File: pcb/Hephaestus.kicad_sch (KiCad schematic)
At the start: 40 parts

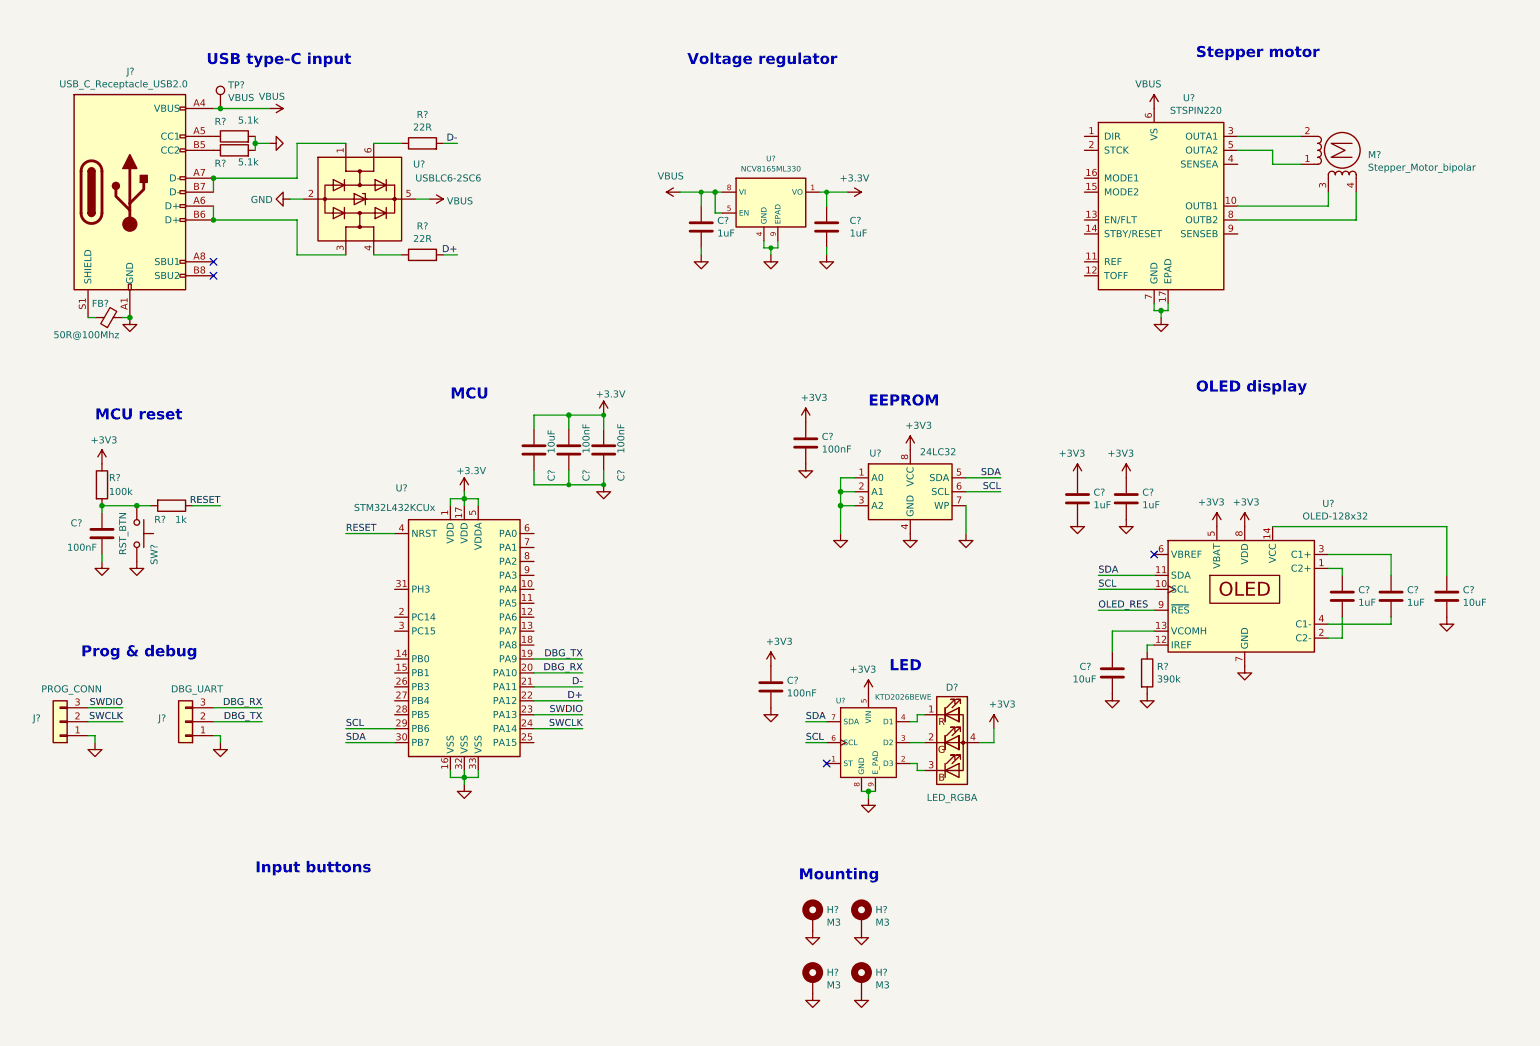
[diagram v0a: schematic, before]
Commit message: Schema: add in put buttons and denoising
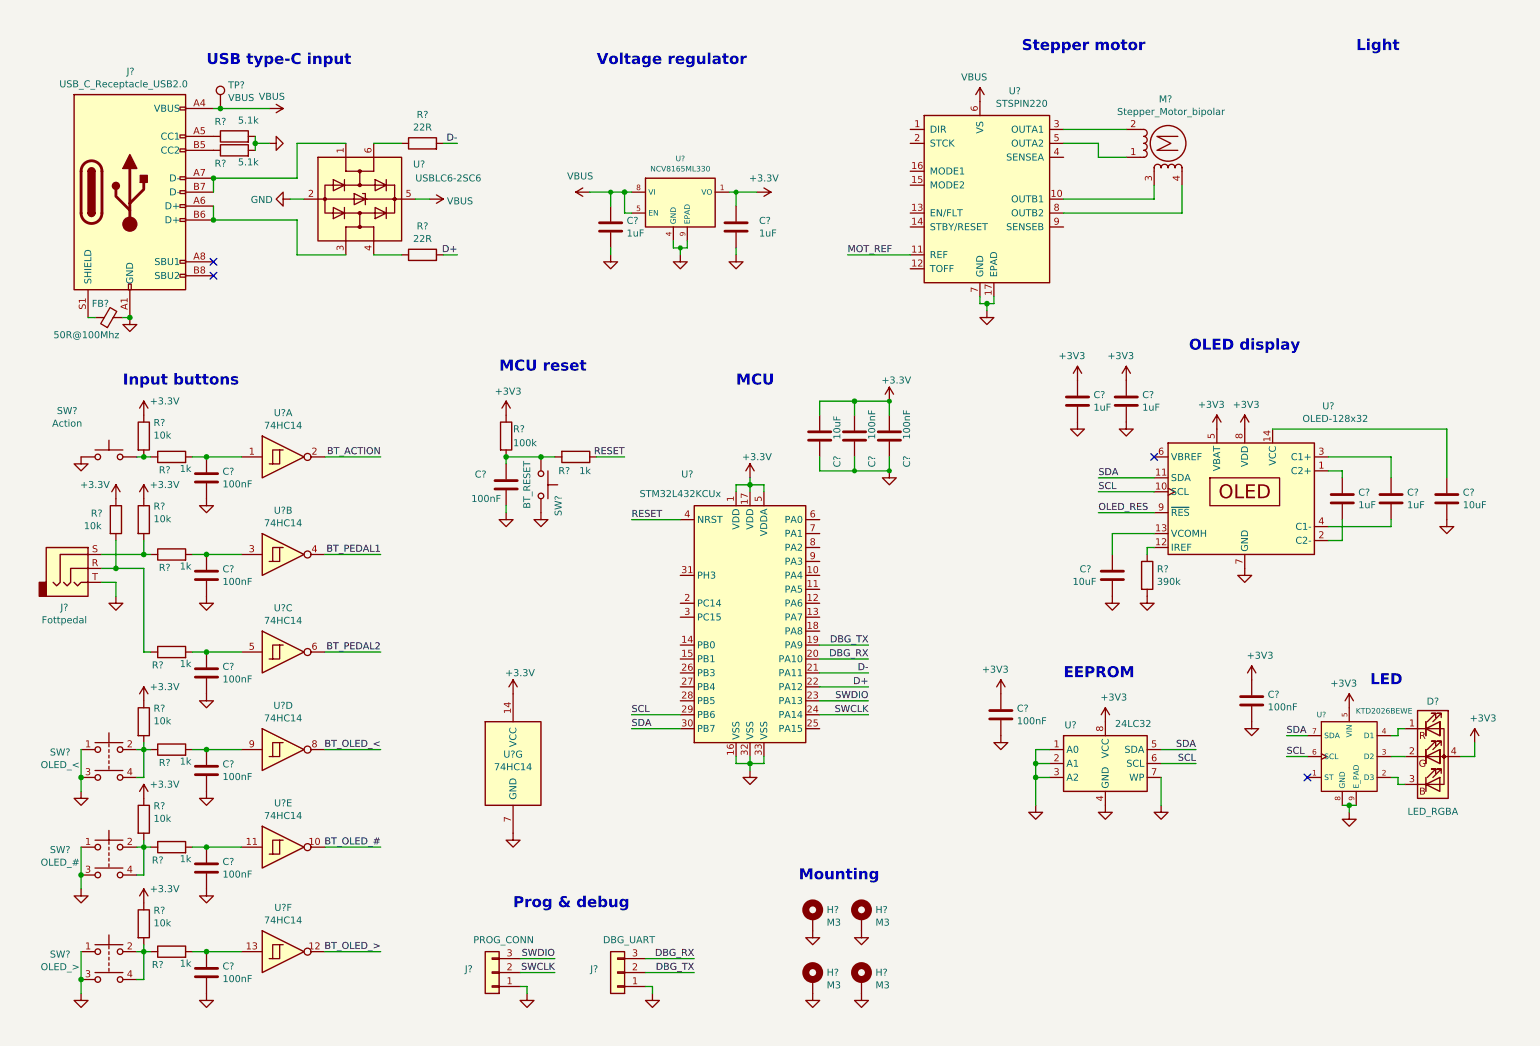
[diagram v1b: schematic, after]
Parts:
- added C? (x6): 100nF, TCY_passives:C_0603_1608Metric, symbol Device:C
- added J?: Fottpedal, Connector_Audio:Jack_3.5mm_CUI_SJ-3523-SMT_Horizontal, symbol Connector:AudioJack3
- added R? (x6): 10k, symbol Device:R
- added R? (x6): 1k, TCY_passives:R_0603_1608Metric, symbol Device:R
- added SW?: OLED_>, symbol Switch:SW_Push_Dual
- added SW?: OLED_<, symbol Switch:SW_Push_Dual
- added SW?: OLED_#, symbol Switch:SW_Push_Dual
- added SW?: Action, symbol Switch:SW_Push
- added U? (x6): 74HC14, symbol 74xx:74HC14
- added U?: 74HC14, Package_DFN_QFN:Texas_S-PVQFN-N14, symbol 74xx:74HC14
- SW?: value RST_BTN -> BT_RESET
- U?: footprint (none) -> TCY_display:OLED_128x32
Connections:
- net +3V3: now also R?.1, R?.1, R?.1, R?.1, R?.1, R?.1, U?.14 (VCC)
- net GND: now also C?.2, C?.2, C?.2, C?.2, C?.2, C?.2, J?.T, SW?.1, SW?.1, SW?.1, SW?.1, SW?.3, SW?.3, SW?.3, U?.7 (GND)
- net MOT_REF: now reaches U?.11 (REF)
- new net: R?.1, R?.2, SW?.2, SW?.4 (x3)
- new net: C?.1, R?.2, U?.9
- new net: C?.1, R?.2, U?.11
- new net: J?.S, R?.1, R?.2
- new net: J?.R, R?.1, R?.2
- new net: C?.1, R?.2, U?.5
- new net: R?.1, R?.2, SW?.2
- new net: C?.1, R?.2, U?.1
- new net: C?.1, R?.2, U?.13
- new net: C?.1, R?.2, U?.3
- new net BT_ACTION: U?.2
- new net BT_OLED_#: U?.10
- new net BT_OLED_<: U?.8
- new net BT_OLED_>: U?.12
- new net BT_PEDAL1: U?.4
- new net BT_PEDAL2: U?.6
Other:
- note added: "Light"
- moved on the sheet: C?, D?, J?, M?, R?, SW?, U?

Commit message: Schema: add light connector
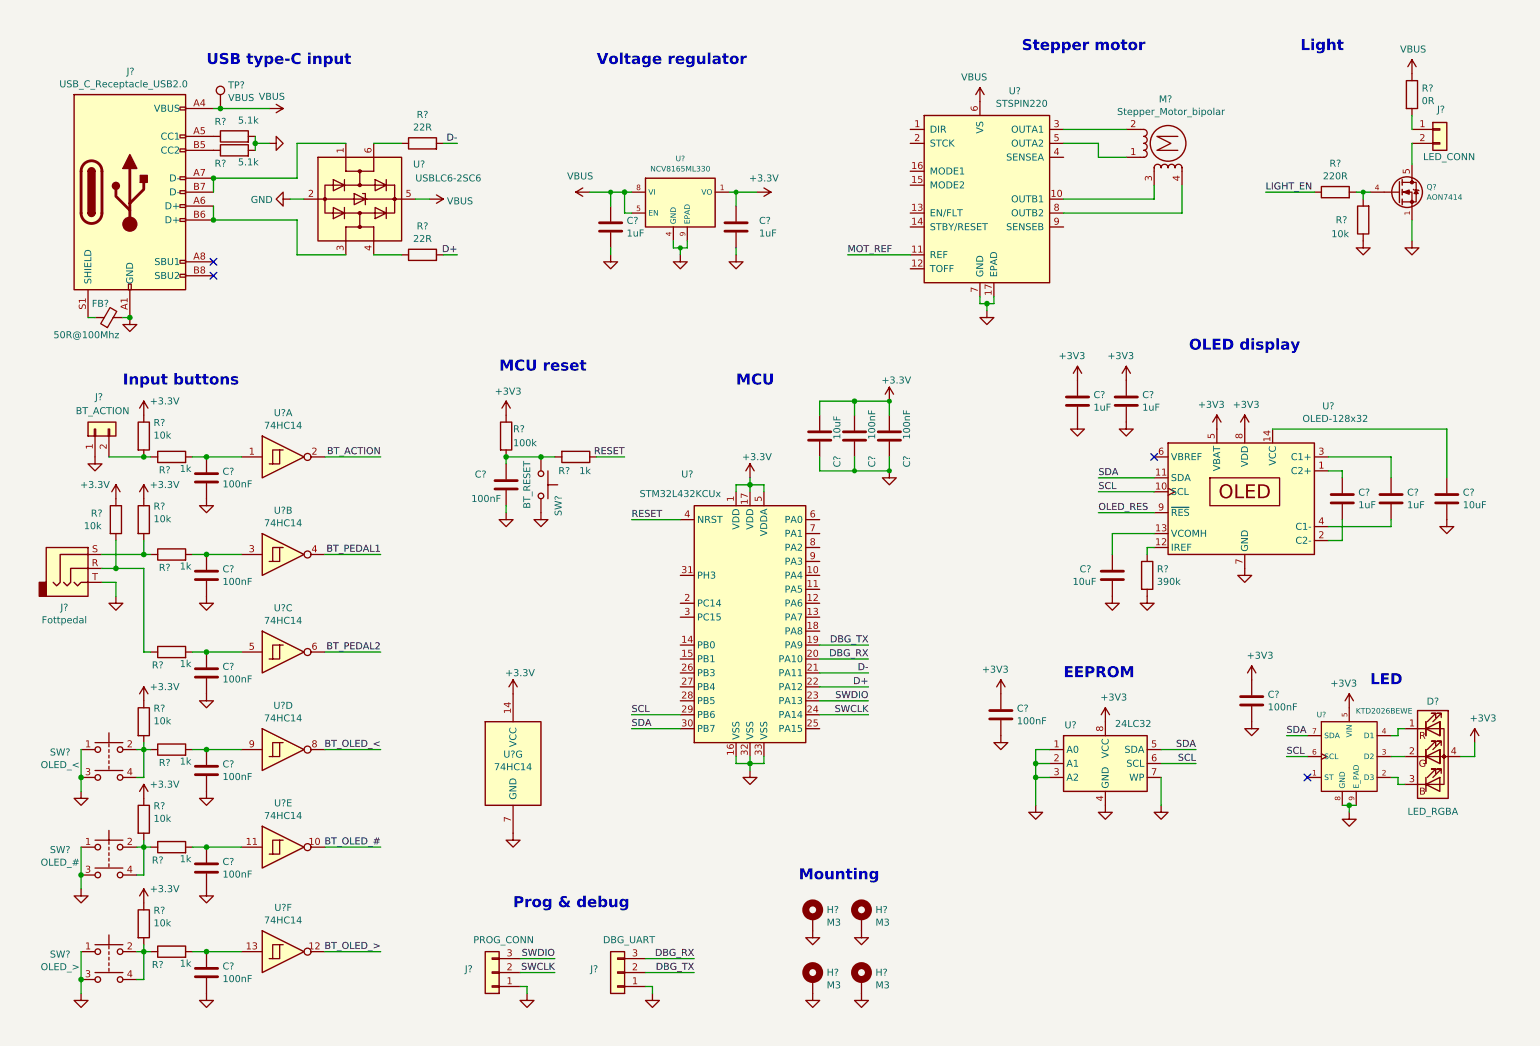
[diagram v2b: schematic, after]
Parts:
- removed SW?: Action, symbol Switch:SW_Push
- added J?: BT_ACTION, symbol Connector_Generic:Conn_01x02
- added J?: LED_CONN, symbol Connector_Generic:Conn_01x02
- added Q?: AON7414, Package_DFN_QFN:DFN-8-1EP_3x3mm_P0.65mm_EP1.55x2.4mm, symbol TCY_transistors:AON7414
- added R?: 220R, symbol Device:R
- added R?: 0R, symbol Device:R
- added R?: 10k, symbol Device:R
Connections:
- net GND: now also J?.1 (Pin_1), Q?.1 (S), Q?.2 (S), Q?.3 (S), R?.1
- net VBUS: now also R?.1
- net at R?.1, R?.2: now also J?.2 (Pin_2)
- new net: Q?.4 (G), R?.2, R?.2
- new net: J?.1 (Pin_1), R?.2
- new net: J?.2 (Pin_2), Q?.5 (D), Q?.6 (D), Q?.7 (D), Q?.8 (D), Q?.9 (D)
- new net LIGHT_EN: R?.1

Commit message: Schema: change stepper motor driver to STPSIN820, add step-up convertor
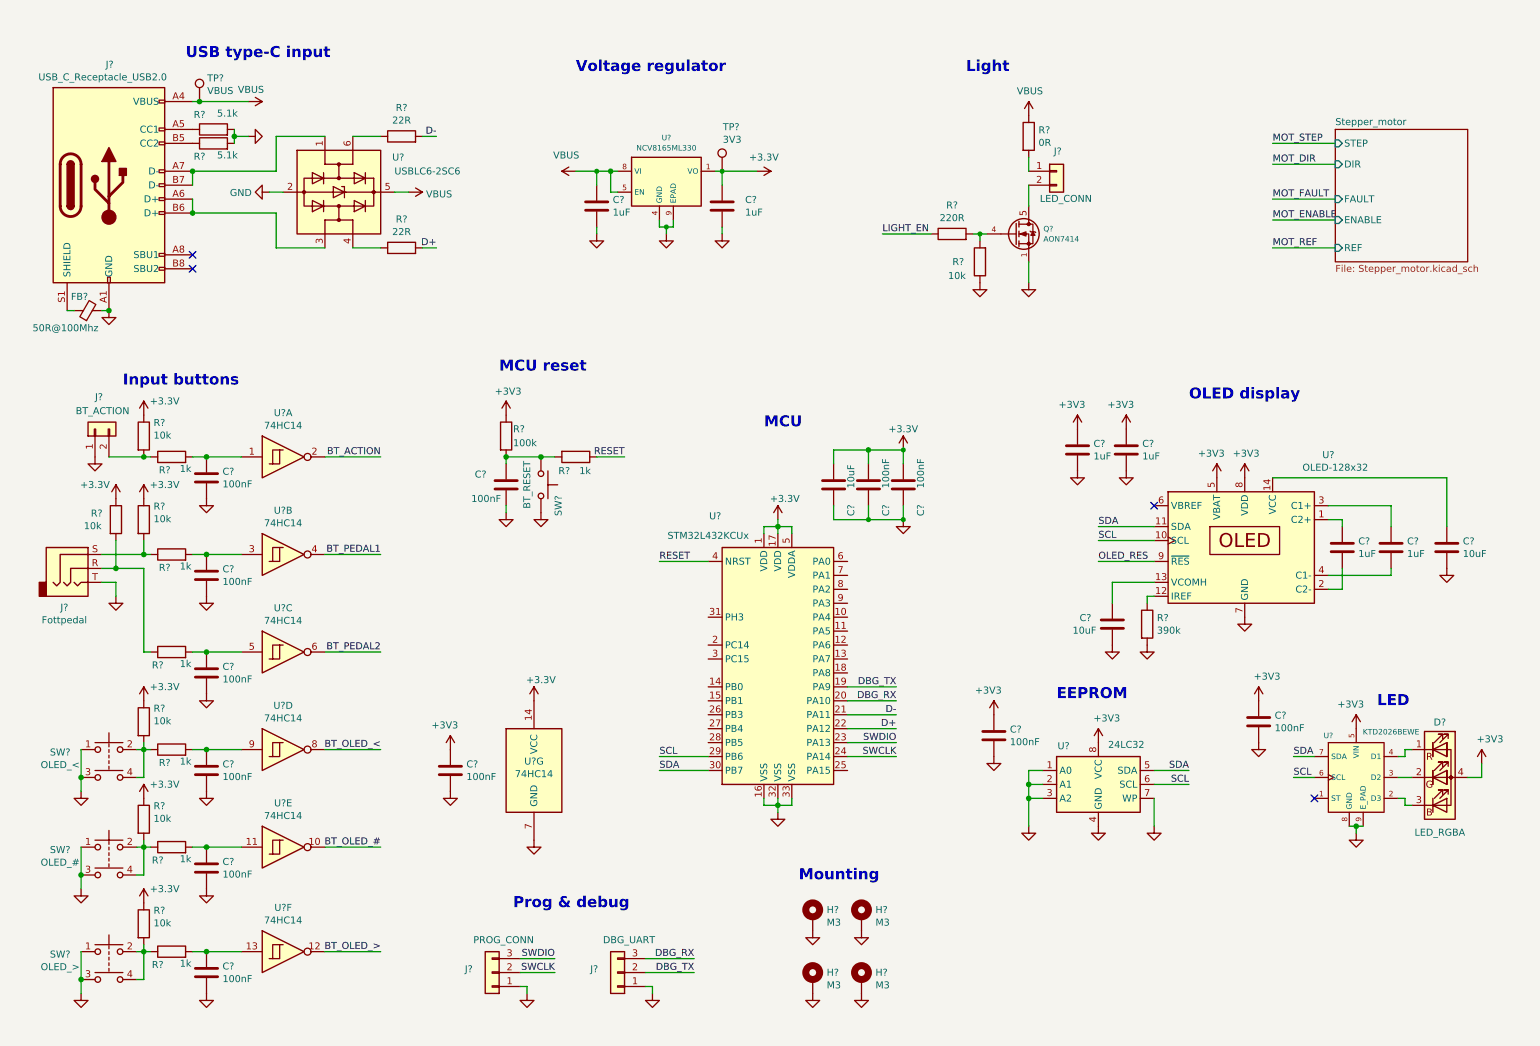
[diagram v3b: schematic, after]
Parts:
- removed M?: Stepper_Motor_bipolar, symbol Motor:Stepper_Motor_bipolar
- removed U?: STSPIN220, Package_DFN_QFN:VQFN-16-1EP_3x3mm_P0.5mm_EP1.8x1.8mm, symbol Driver_Motor:STSPIN220
- added C?: 100nF, symbol Device:C
- added TP?: 3V3, TCY_connectors:TestPoint_Pad_D0.5mm, symbol Connector:TestPoint
- R?: footprint (none) -> Resistor_SMD:R_1206_3216Metric
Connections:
- net +3V3: now also C?.1, TP?.1
- net GND: now also C?.2
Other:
- added sheet Stepper_motor (Stepper_motor.kicad_sch)
- note removed: "Stepper motor"
- moved on the sheet: C?, D?, FB?, J?, Q?, R?, TP?, U?, U?G

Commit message: Schema: connect MCU to buttons and stepper motor
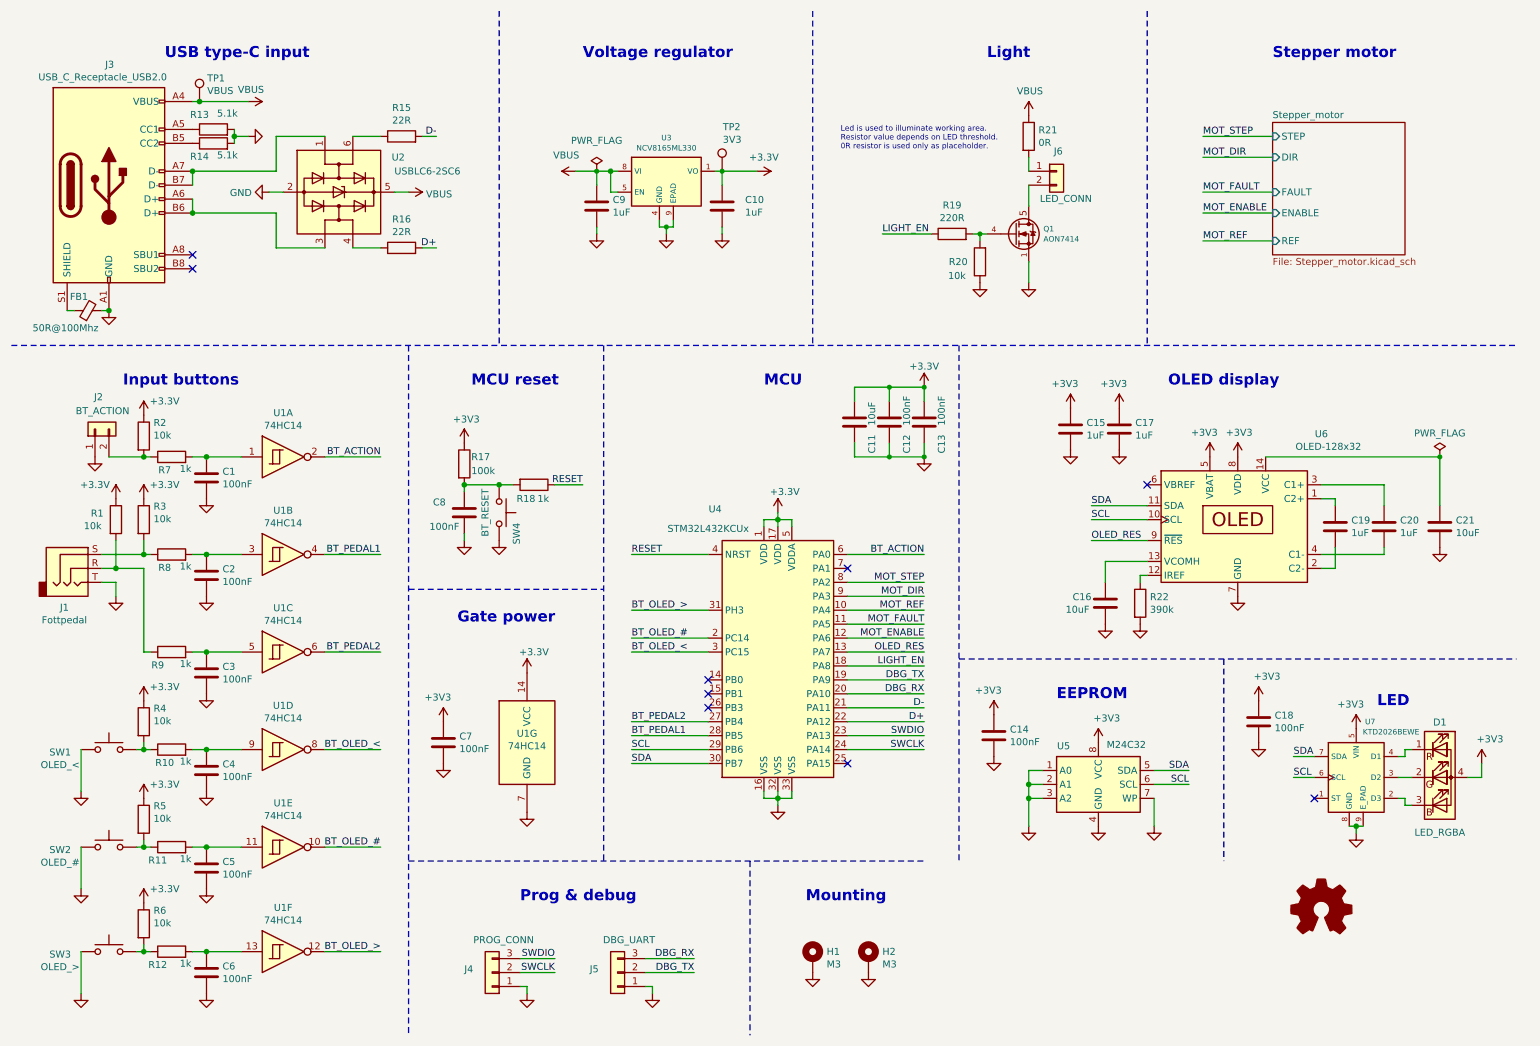
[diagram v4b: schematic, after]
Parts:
- removed H? (x2): M3, symbol Mechanical:MountingHole_Pad
- C15, C17, C19, C20, C7: renamed from C?; footprint (none) -> Capacitor_SMD:C_0603_1608Metric
- C16, C21: renamed from C?; footprint (none) -> Capacitor_SMD:C_0805_2012Metric
- H1, H2: renamed from H?; footprint (none) -> MountingHole:MountingHole_3.2mm_M3_Pad_Via
- J2, J6: renamed from J?; footprint (none) -> TCY_connectors:Amphenol_10114830-11102LF_1x02_P1.25mm_Horizontal
- R1, R19, R2, R20, R22, R3, R4, R5, R6: renamed from R?; footprint (none) -> Resistor_SMD:R_0603_1608Metric
- R10, R11, R12, R7, R8, R9: renamed from R?; footprint TCY_passives:R_0603_1608Metric -> Resistor_SMD:R_0603_1608Metric
- SW1, SW2, SW3: renamed from SW?; footprint (none) -> Button_Switch_SMD:SW_SPST_TL3305A; symbol Switch:SW_Push_Dual -> Switch:SW_Push
- U1: renamed from U?; footprint (none) -> Package_DFN_QFN:Texas_S-PVQFN-N14
- U5: renamed from U?; value 24LC32 -> M24C32
- U7: renamed from U?; symbol TCY_IC:KTD2026BEWE -> TCY_LEDs:KTD2026BEWE
- gave numbers to parts that had none: 36
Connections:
- net BT_ACTION: now also U4.6 (PA0)
- net BT_OLED_#: now also U4.2 (PC14)
- net BT_OLED_<: now also U4.3 (PC15)
- net BT_OLED_>: now also U4.31 (PH3)
- net BT_PEDAL1: now also U4.28 (PB5)
- net BT_PEDAL2: now also U4.27 (PB4)
- net GND: no longer SW1.3, SW2.3, SW3.3
- net LIGHT_EN: now also U4.18 (PA8)
- net MOT_DIR: now also U4.9 (PA3)
- net MOT_ENABLE: now also U4.12 (PA6)
- net MOT_FAULT: now also U4.11 (PA5)
- net MOT_REF: now also U4.10 (PA4)
- net MOT_STEP: now also U4.8 (PA2)
- net OLED_RES: now also U4.13 (PA7)
- net at R12.1, R6.2, SW3.2: no longer SW3.4
- net at R10.1, R4.2, SW1.2: no longer SW1.4
- net at R11.1, R5.2, SW2.2: no longer SW2.4
- no-connect marks 4 -> 9
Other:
- note added: "Gate power"
- note added: "Led is used to illuminate working area. Resistor value depends on LED threshold. 0R resistor is used only as placeholder."
- note added: "Stepper motor"
- company: (none) -> Author: Petr Malaník
- title: (none) -> Hepheatus - Solder paste dispensor
- moved on the sheet: C11, C12, C13, C15, C16, C17, C19, C20, C21, C7, C8, H1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
